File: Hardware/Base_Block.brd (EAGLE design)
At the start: 30.5 x 44.5 mm, 48 parts, among them Q1 BSS138, U2 FTS31XS-U, U4 TPS62065

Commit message: file cleanup
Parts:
- L1: value (none) -> 1.0uH
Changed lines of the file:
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@@
 <attribute name="PROD_ID" value="CAP-08280" x="13.843" y="12.065" size="1.778" layer="27" display="off"/>
 </element>
-<element name="L1" library="SparkFun-Passives" package="INDUCTOR-SRP4020" value="" x="16.002" y="19.177"/>
+<element name="L1" library="SparkFun-Passives" package="INDUCTOR-SRP4020" value="1.0uH" x="16.002" y="19.177"/>
 <element name="LOGO1" library="SparkFun-Aesthetics" package="SFE_LOGO_NAME_FLAME_.1" value="SFE_LOGO_NAME_FLAME.1_INCH" x="9.271" y="0.254"/>
 <element name="LOGO4" library="SparkFun-Aesthetics" package="OSHW-LOGO-S" value="OSHW-LOGOS" x="5.842" y="1.778"/>
@@
 <contactref element="U3" pad="GND1"/>
 <via x="16.9418" y="27.813" extent="1-16" drill="0.508"/>
-<via x="24.511" y="24.638" extent="1-16" drill="0.508"/>
-<via x="25.273" y="23.876" extent="1-16" drill="0.508"/>
+<via x="24.765" y="24.765" extent="1-16" drill="0.508"/>
+<via x="25.781" y="24.257" extent="1-16" drill="0.508"/>
 <contactref element="C8" pad="2"/>
 <contactref element="U$1" pad="2"/>
@@
 <wire x1="24.638" y1="20.32" x2="24.0978" y2="19.7798" width="0.1524" layer="1"/>
 <wire x1="24.0978" y1="19.7798" x2="23.32" y2="19.7798" width="0.1524" layer="1"/>
-<wire x1="24.638" y1="20.32" x2="24.638" y2="23.368" width="0.1524" layer="1"/>
+<wire x1="24.638" y1="20.32" x2="24.638" y2="23.622" width="0.1524" layer="1"/>
 <wire x1="19.446" y1="37.48" x2="20.716" y2="38.75" width="0.1524" layer="1"/>
 <wire x1="20.716" y1="38.75" x2="20.716" y2="39.464" width="0.1524" layer="1"/>
 <wire x1="19.446" y1="26.909" x2="21.209" y2="25.146" width="0.1524" layer="1"/>
-<wire x1="21.209" y1="25.146" x2="22.86" y2="25.146" width="0.1524" layer="1"/>
-<wire x1="22.86" y1="25.146" x2="24.638" y2="23.368" width="0.1524" layer="1"/>
+<wire x1="21.209" y1="25.146" x2="23.114" y2="25.146" width="0.1524" layer="1"/>
+<wire x1="23.114" y1="25.146" x2="24.638" y2="23.622" width="0.1524" layer="1"/>
 <wire x1="19.446" y1="37.48" x2="19.446" y2="26.909" width="0.1524" layer="1"/>
 <wire x1="19.7612" y1="21.0312" x2="19.7612" y2="21.1582" width="0.1524" layer="16"/>
@@
 <contactref element="U$3" pad="16"/>
 <contactref element="U3" pad="D+1"/>
-<wire x1="24.257" y1="23.241" x2="24.257" y2="20.447" width="0.1524" layer="1"/>
+<wire x1="24.257" y1="23.495" x2="24.257" y2="20.447" width="0.1524" layer="1"/>
 <wire x1="24.257" y1="20.447" x2="23.9898" y2="20.1798" width="0.1524" layer="1"/>
 <wire x1="23.32" y1="20.1798" x2="23.9898" y2="20.1798" width="0.1524" layer="1"/>
@@
 <wire x1="20.066" y1="38.608" x2="20.066" y2="39.464" width="0.1524" layer="1"/>
 <wire x1="19.05" y1="26.797" x2="21.082" y2="24.765" width="0.1524" layer="1"/>
-<wire x1="21.082" y1="24.765" x2="22.733" y2="24.765" width="0.1524" layer="1"/>
-<wire x1="22.733" y1="24.765" x2="24.257" y2="23.241" width="0.1524" layer="1"/>
+<wire x1="21.082" y1="24.765" x2="22.987" y2="24.765" width="0.1524" layer="1"/>
+<wire x1="22.987" y1="24.765" x2="24.257" y2="23.495" width="0.1524" layer="1"/>
 </signal>
 <signal name="USB_ID">

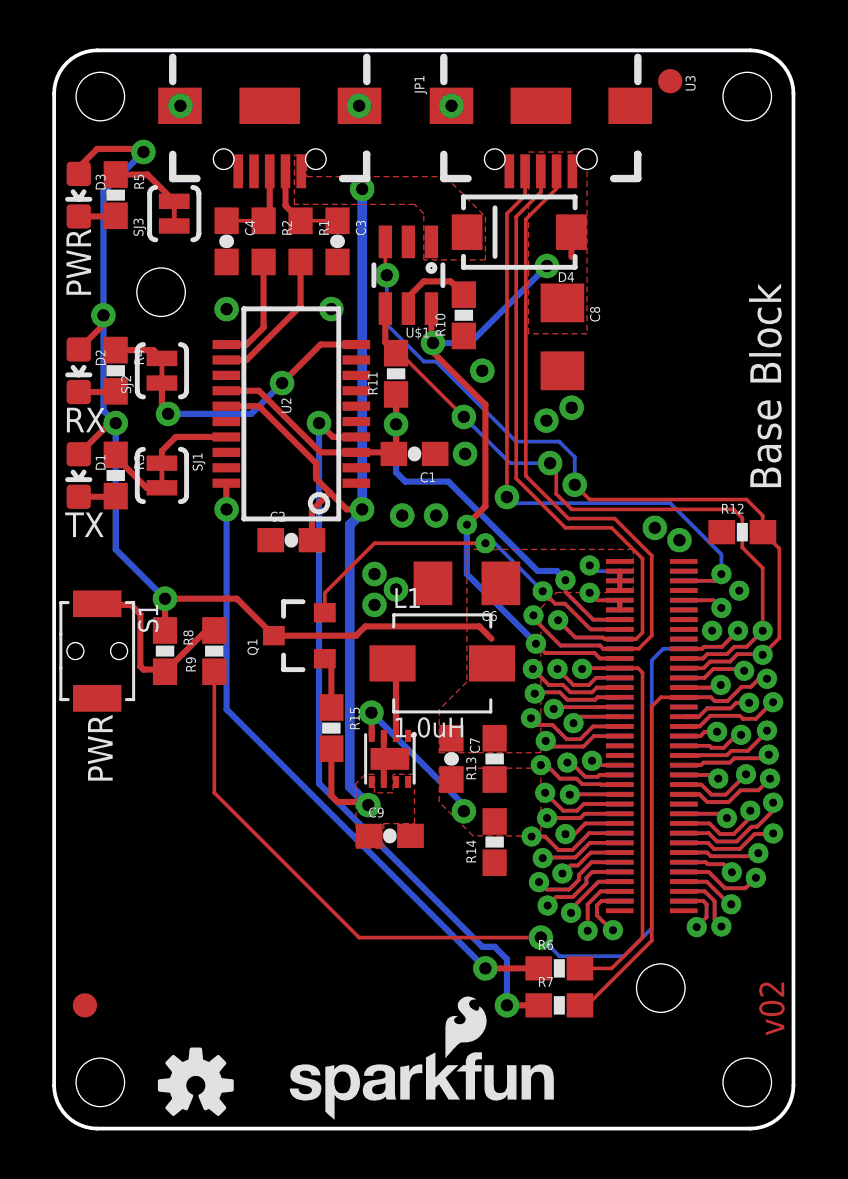
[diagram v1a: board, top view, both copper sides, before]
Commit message: Modified Footprint for connectors, removed jumpers. changed version number corrected silk moved diode to help AOI removed jumpers from power supply replaced input and output capacitors on power supply. replaced filtercap with 47pf
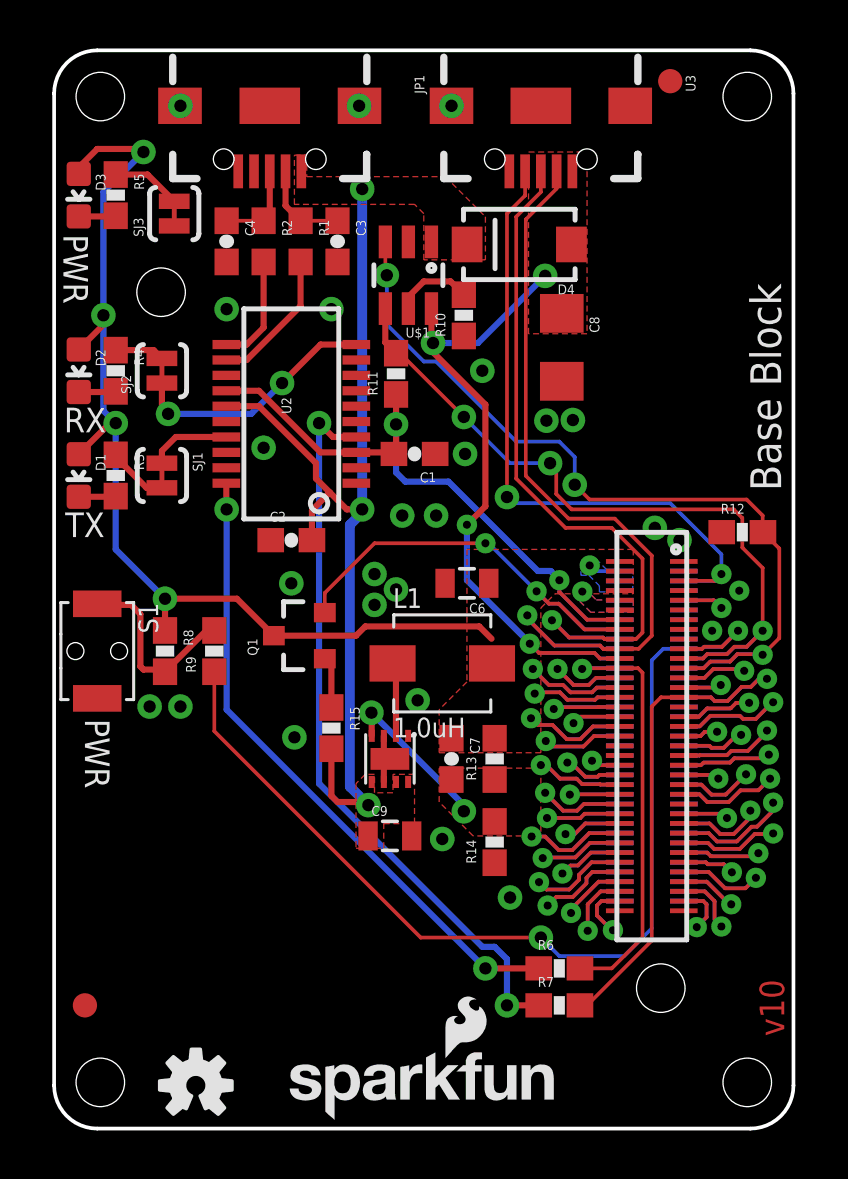
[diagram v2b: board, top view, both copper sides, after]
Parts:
- C6: value 10uF -> 22uF; device SparkFun-Capacitors:1206 -> SparkFun-Capacitors:0805
- C7: value 9.0pF -> 47pF
- C9: value 4.7uF -> 22uF; device SparkFun-Capacitors:0603-CAP -> SparkFun-Capacitors:0805
- moved D4 0.51 mm to (19.2, 36.4)
- moved C8 0.43 mm to (20.9, 32.2)
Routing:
- net 3.3V: track 3.94 -> 0.00 mm
- net VSYS: track 46.4 -> 44.4 mm
- net PWRBTN#: track 44.0 -> 42.5 mm
- net USB_DP: track 29.5 -> 30.0 mm
- net USB_DN: track 32.9 -> 33.4 mm
- net GND: vias 18 -> 26
- added copper zone on layer 1, net 3.3V
- added copper zone on layer 16, net 3.3V
- added copper zone on layer 16, net VSYS
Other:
- board text added: "v10"
- board text removed: "v02"
